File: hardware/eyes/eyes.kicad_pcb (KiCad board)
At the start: 2 copper layers, 130 x 95 mm, 1 part

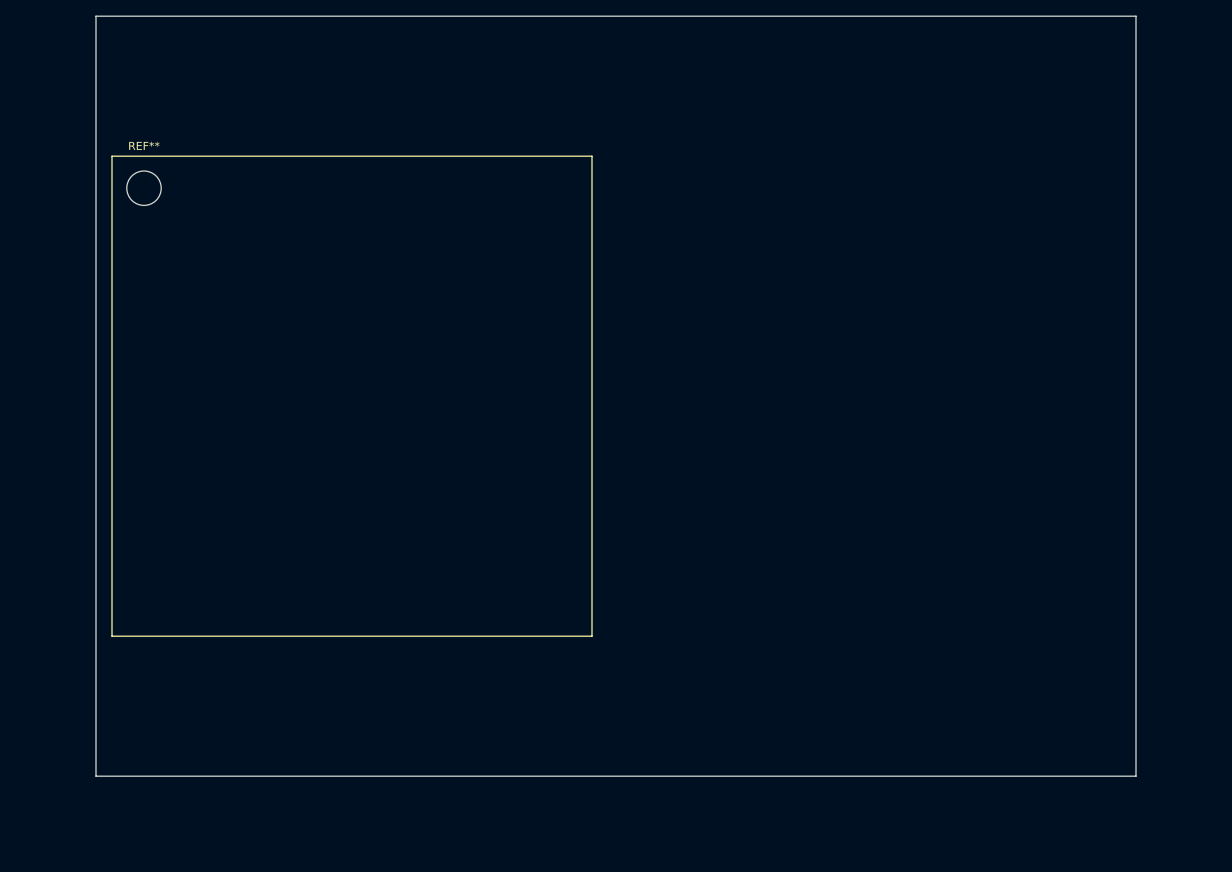
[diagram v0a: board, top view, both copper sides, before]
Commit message: Finishing eyes board schematics, and PCB
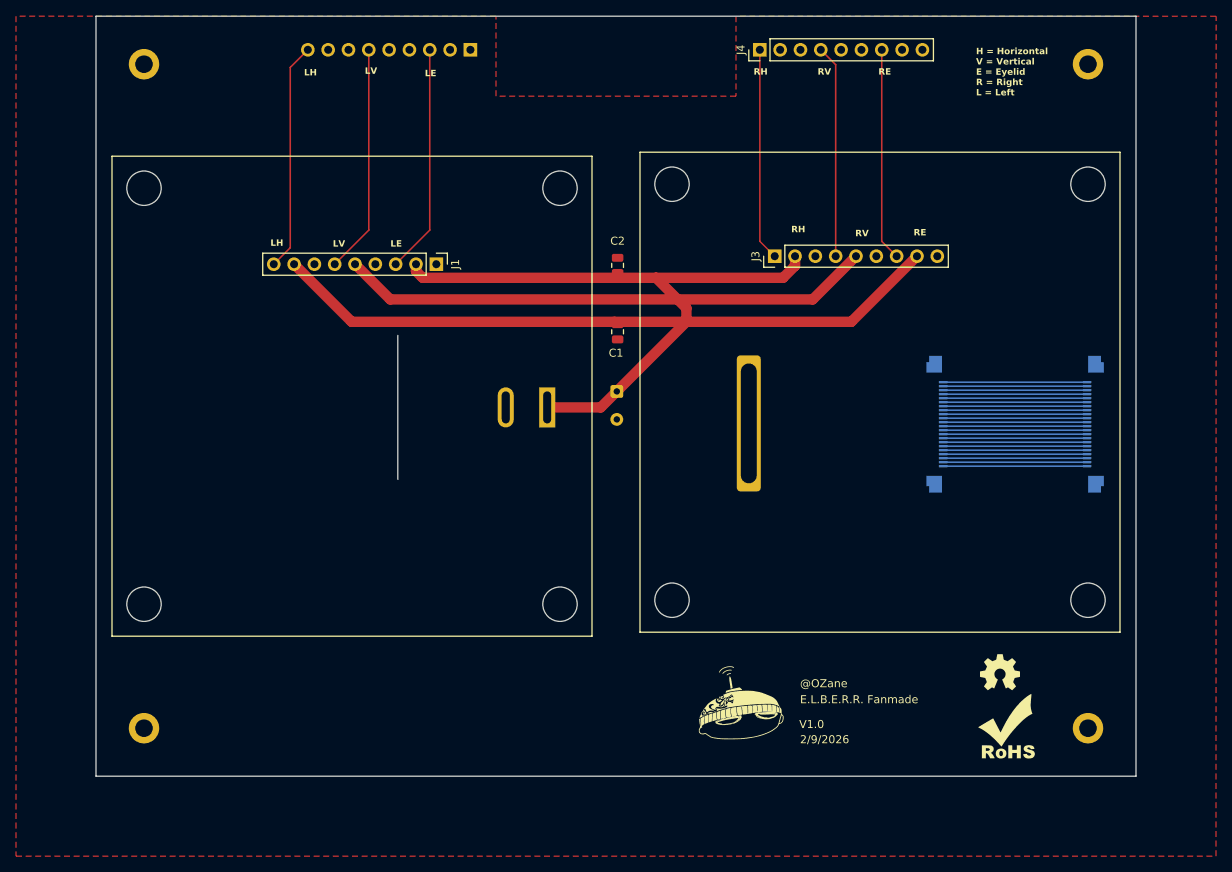
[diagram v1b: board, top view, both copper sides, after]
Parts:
- added C1: 0.1uF, Capacitor_SMD:C_0805_2012Metric, F.Cu at (145.2, 88.4)
- added C2: 0.1uF, Capacitor_SMD:C_0805_2012Metric, F.Cu at (145.2, 80.1)
- added C7: 100uF, Capacitor_THT:CP_Radial_D8.0mm_P3.50mm, B.Cu at (145.1, 95.8)
- added G***: LOGO, LOGO, F.Cu at (102.0, 135.9)
- added G***: LOGO, LOGO, F.Cu at (194.0, 137.9)
- added G***: LOGO, LOGO, F.Cu at (161.0, 136.9)
- added G***: LOGO, LOGO, F.Cu at (193.0, 130.9)
- added J1: Conn_01x09_Pin, Connector_PinHeader_2.54mm:PinHeader_1x09_P2.54mm_Vertical, F.Cu at (122.6, 79.9)
- added J2: Conn_01x09_Pin, Connector_PinHeader_2.54mm:PinHeader_1x09_P2.54mm_Vertical, B.Cu at (126.8, 53.1)
- added J3: Conn_01x09_Pin, Connector_PinHeader_2.54mm:PinHeader_1x09_P2.54mm_Vertical, F.Cu at (164.9, 78.9)
- added J4: Conn_01x09_Pin, Connector_PinHeader_2.54mm:PinHeader_1x09_P2.54mm_Vertical, F.Cu at (163.0, 53.1)
- added J5: Barrel_Jack, Connector_BarrelJack:BarrelJack_SwitchcraftConxall_RAPC10U_Horizontal, B.Cu at (136.4, 97.8)
- added J8: Conn_01x22, Connector_FFC-FPC:Amphenol_F32Q-1A7x1-11022_1x22-1MP_P0.5mm_Horizontal, B.Cu at (183.0, 99.9)
- added J9: Conn_01x22, Connector_FFC-FPC:Amphenol_F32Q-1A7x1-11022_1x22-1MP_P0.5mm_Horizontal, B.Cu at (206.8, 99.9)
- added REF**: MountingHole_2.2mm_M2_DIN965_Pad, MountingHole:MountingHole_2.2mm_M2_DIN965_Pad, F.Cu at (86.0, 137.9)
- added REF**: MountingHole_4.3mm_M4, MountingHole:MountingHole_4.3mm_M4, F.Cu at (86.0, 122.4)
- added REF**: MountingHole_4.3mm_M4, MountingHole:MountingHole_4.3mm_M4, F.Cu at (204.0, 121.9)
- added REF**: MountingHole_4.3mm_M4, MountingHole:MountingHole_4.3mm_M4, F.Cu at (204.0, 69.9)
- added REF**: hole, MountingHole:hole, F.Cu at (161.6, 99.8)
- added REF**: MountingHole_4.3mm_M4, MountingHole:MountingHole_4.3mm_M4, F.Cu at (152.0, 121.9)
- added REF**: MountingHole_2.2mm_M2_DIN965_Pad, MountingHole:MountingHole_2.2mm_M2_DIN965_Pad, F.Cu at (204.0, 137.9)
- added REF**: MountingHole_2.2mm_M2_DIN965_Pad, MountingHole:MountingHole_2.2mm_M2_DIN965_Pad, F.Cu at (86.0, 54.9)
- added REF**: MountingHole_2.2mm_M2_DIN965_Pad, MountingHole:MountingHole_2.2mm_M2_DIN965_Pad, F.Cu at (204.0, 54.9)
- added REF**: MountingHole_4.3mm_M4, MountingHole:MountingHole_4.3mm_M4, F.Cu at (138.0, 122.4)
- added REF**: MountingHole_4.3mm_M4, MountingHole:MountingHole_4.3mm_M4, F.Cu at (138.0, 70.4)
- added REF**: MountingHole_4.3mm_M4, MountingHole:MountingHole_4.3mm_M4, F.Cu at (152.0, 69.9)
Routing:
- net +5V: track 0.00 -> 230.2 mm
- net LE: track 0.00 -> 28.6 mm
- net LH: track 0.00 -> 28.6 mm
- net LV: track 0.00 -> 28.6 mm
- net RV: track 0.00 -> 26.6 mm
- net RH: track 0.00 -> 26.6 mm
- net RE: track 0.00 -> 26.6 mm
- net Net-(J8-Pin_9): track 0.00 -> 18.0 mm
- net Net-(J8-Pin_8): track 0.00 -> 18.0 mm
- net Net-(J8-Pin_7): track 0.00 -> 18.0 mm
- net Net-(J8-Pin_6): track 0.00 -> 18.0 mm
- net Net-(J8-Pin_5): track 0.00 -> 18.0 mm
- net Net-(J8-Pin_4): track 0.00 -> 18.0 mm
- net Net-(J8-Pin_3): track 0.00 -> 18.0 mm
- net Net-(J8-Pin_22): track 0.00 -> 18.0 mm
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- added copper zone on F.Cu, net GND
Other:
- board text added: "2/9/2026"
- board text added: "@LIGHTSAREOFF"
- board text added: "@OZane"
- board text added: "E.L.B.E.R.R. Fanmade"
- board text added: "H = Horizontal V = Vertical E = Eyelid R = Right L = Left"
- board text added: "LE"
- board text added: "LH"
- board text added: "LV"
- board text added: "RE"
- board text added: "RH"
- board text added: "RV"
- board text added: "V1.0"
- board text added: "original serie from"

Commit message: Finishing eyes PCB and exporting BOM
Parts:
- J4: moved to B.Cu
- J5: footprint Connector_BarrelJack:BarrelJack_SwitchcraftConxall_RAPC10U_Horizontal -> Connector_BarrelJack:BarrelJack_Horizontal
- moved J4 20.3 mm to (183.3, 53.0)
- moved J3 20.3 mm to (185.2, 78.9), turned to -90 degrees
- moved J5 1.75 mm to (134.7, 97.9)
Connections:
- J8 pad MP: (no net) -> GND
- J9 pad MP: (no net) -> GND
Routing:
- net GND: vias 0 -> 180
- added copper zone on B.Cu, net GND
